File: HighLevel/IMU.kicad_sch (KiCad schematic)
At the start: 8 parts, among them U1 MPU-9150

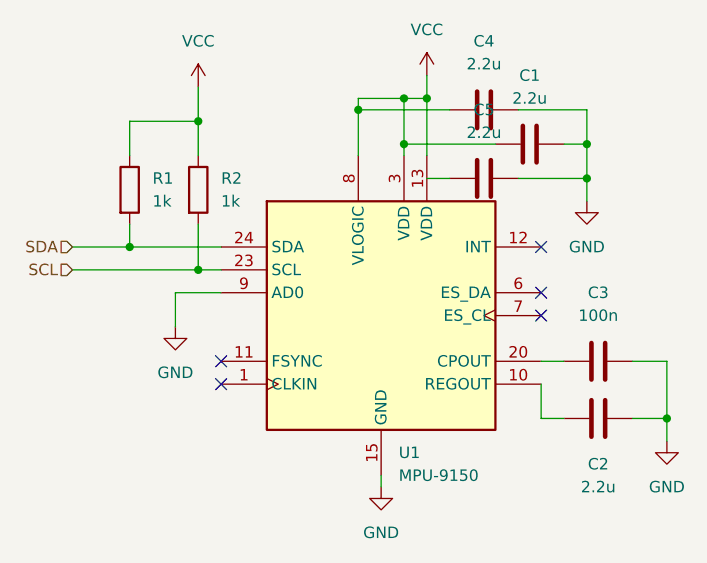
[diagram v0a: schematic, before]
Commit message: Arranged components on PCB
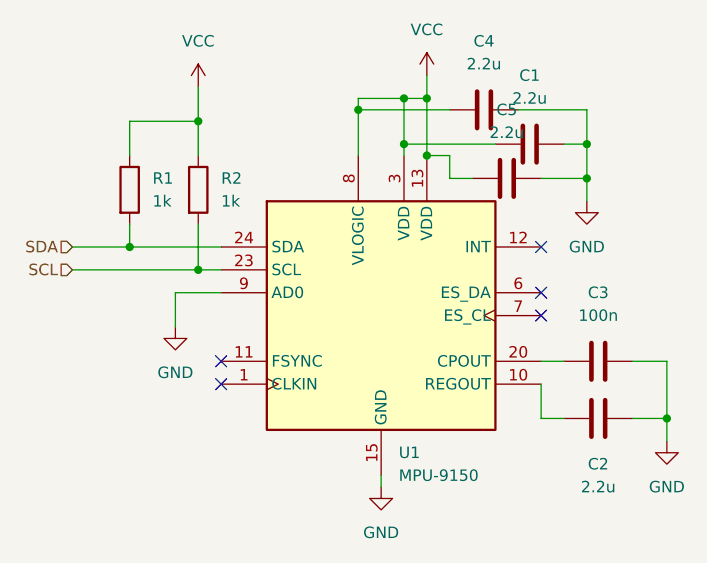
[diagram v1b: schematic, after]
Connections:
- net VCC: now also C5.1
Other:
- moved on the sheet: C5
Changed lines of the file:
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@@
   (junction (at 182.88 76.2) (diameter 0) (color 0 0 0 0)
+  )
+  (junction (at 165.1 73.66) (diameter 0) (color 0 0 0 0)
   )
   (junction (at 182.88 72.39) (diameter 0) (color 0 0 0 0)
@@
     (stroke (width 0) (type default))
   )
-  (wire (pts (xy 165.1 76.2) (xy 167.64 76.2))
+  (wire (pts (xy 167.64 76.2) (xy 170.18 76.2))
+    (stroke (width 0) (type default))
+  )
+  (wire (pts (xy 137.16 88.9) (xy 142.24 88.9))
+    (stroke (width 0) (type default))
+  )
+  (wire (pts (xy 139.7 81.28) (xy 139.7 86.36))
+    (stroke (width 0) (type default))
+  )
+  (wire (pts (xy 132.08 73.66) (xy 132.08 69.85))
+    (stroke (width 0) (type default))
+  )
+  (wire (pts (xy 162.56 67.31) (xy 165.1 67.31))
+    (stroke (width 0) (type default))
+  )
+  (wire (pts (xy 162.56 67.31) (xy 162.56 72.39))
+    (stroke (width 0) (type default))
+  )
+  (wire (pts (xy 182.88 76.2) (xy 182.88 78.74))
+    (stroke (width 0) (type default))
+  )
+  (wire (pts (xy 177.8 76.2) (xy 182.88 76.2))
+    (stroke (width 0) (type default))
+  )
+  (wire (pts (xy 177.8 102.87) (xy 180.34 102.87))
+    (stroke (width 0) (type default))
+  )
+  (wire (pts (xy 132.08 83.82) (xy 142.24 83.82))
+    (stroke (width 0) (type default))
+  )
+  (wire (pts (xy 132.08 69.85) (xy 139.7 69.85))
+    (stroke (width 0) (type default))
+  )
+  (wire (pts (xy 137.16 92.71) (xy 137.16 88.9))
+    (stroke (width 0) (type default))
+  )
+  (wire (pts (xy 132.08 81.28) (xy 132.08 83.82))
+    (stroke (width 0) (type default))
+  )
+  (wire (pts (xy 175.26 68.58) (xy 182.88 68.58))
+    (stroke (width 0) (type default))
+  )
+  (wire (pts (xy 157.48 67.31) (xy 157.48 68.58))
+    (stroke (width 0) (type default))
+  )
+  (wire (pts (xy 139.7 66.04) (xy 139.7 69.85))
+    (stroke (width 0) (type default))
+  )
+  (wire (pts (xy 177.8 99.06) (xy 177.8 102.87))
+    (stroke (width 0) (type default))
+  )
+  (wire (pts (xy 191.77 96.52) (xy 191.77 102.87))
+    (stroke (width 0) (type default))
+  )
+  (wire (pts (xy 182.88 68.58) (xy 182.88 72.39))
+    (stroke (width 0) (type default))
+  )
+  (wire (pts (xy 182.88 72.39) (xy 182.88 76.2))
+    (stroke (width 0) (type default))
+  )
+  (wire (pts (xy 187.96 102.87) (xy 191.77 102.87))
+    (stroke (width 0) (type default))
+  )
+  (wire (pts (xy 162.56 72.39) (xy 162.56 73.66))
+    (stroke (width 0) (type default))
+  )
+  (wire (pts (xy 165.1 64.77) (xy 165.1 67.31))
+    (stroke (width 0) (type default))
+  )
+  (wire (pts (xy 157.48 68.58) (xy 167.64 68.58))
+    (stroke (width 0) (type default))
+  )
+  (wire (pts (xy 191.77 102.87) (xy 191.77 105.41))
+    (stroke (width 0) (type default))
+  )
+  (wire (pts (xy 167.64 73.66) (xy 167.64 76.2))
+    (stroke (width 0) (type default))
+  )
+  (wire (pts (xy 157.48 67.31) (xy 162.56 67.31))
     (stroke (width 0) (type default))
   )
@@
     (stroke (width 0) (type default))
   )
-  (wire (pts (xy 137.16 88.9) (xy 142.24 88.9))
-    (stroke (width 0) (type default))
-  )
-  (wire (pts (xy 139.7 81.28) (xy 139.7 86.36))
-    (stroke (width 0) (type default))
-  )
-  (wire (pts (xy 132.08 73.66) (xy 132.08 69.85))
-    (stroke (width 0) (type default))
-  )
-  (wire (pts (xy 162.56 67.31) (xy 165.1 67.31))
-    (stroke (width 0) (type default))
-  )
-  (wire (pts (xy 162.56 67.31) (xy 162.56 72.39))
-    (stroke (width 0) (type default))
-  )
-  (wire (pts (xy 182.88 76.2) (xy 182.88 78.74))
-    (stroke (width 0) (type default))
-  )
-  (wire (pts (xy 175.26 76.2) (xy 182.88 76.2))
-    (stroke (width 0) (type default))
-  )
-  (wire (pts (xy 177.8 102.87) (xy 180.34 102.87))
-    (stroke (width 0) (type default))
-  )
-  (wire (pts (xy 132.08 83.82) (xy 142.24 83.82))
-    (stroke (width 0) (type default))
-  )
-  (wire (pts (xy 132.08 69.85) (xy 139.7 69.85))
-    (stroke (width 0) (type default))
-  )
-  (wire (pts (xy 137.16 92.71) (xy 137.16 88.9))
-    (stroke (width 0) (type default))
-  )
-  (wire (pts (xy 132.08 81.28) (xy 132.08 83.82))
-    (stroke (width 0) (type default))
-  )
-  (wire (pts (xy 175.26 68.58) (xy 182.88 68.58))
-    (stroke (width 0) (type default))
-  )
-  (wire (pts (xy 157.48 67.31) (xy 157.48 68.58))
-    (stroke (width 0) (type default))
-  )
-  (wire (pts (xy 139.7 66.04) (xy 139.7 69.85))
-    (stroke (width 0) (type default))
-  )
-  (wire (pts (xy 177.8 99.06) (xy 177.8 102.87))
-    (stroke (width 0) (type default))
-  )
-  (wire (pts (xy 191.77 96.52) (xy 191.77 102.87))
-    (stroke (width 0) (type default))
-  )
-  (wire (pts (xy 182.88 68.58) (xy 182.88 72.39))
-    (stroke (width 0) (type default))
-  )
-  (wire (pts (xy 182.88 72.39) (xy 182.88 76.2))
-    (stroke (width 0) (type default))
-  )
-  (wire (pts (xy 187.96 102.87) (xy 191.77 102.87))
-    (stroke (width 0) (type default))
-  )
-  (wire (pts (xy 162.56 72.39) (xy 162.56 73.66))
-    (stroke (width 0) (type default))
-  )
-  (wire (pts (xy 165.1 64.77) (xy 165.1 67.31))
-    (stroke (width 0) (type default))
-  )
-  (wire (pts (xy 157.48 68.58) (xy 167.64 68.58))
-    (stroke (width 0) (type default))
-  )
-  (wire (pts (xy 191.77 102.87) (xy 191.77 105.41))
-    (stroke (width 0) (type default))
-  )
-  (wire (pts (xy 157.48 67.31) (xy 162.56 67.31))
-    (stroke (width 0) (type default))
-  )
   (wire (pts (xy 125.73 86.36) (xy 139.7 86.36))
     (stroke (width 0) (type default))
@@
     (stroke (width 0) (type default))
   )
+  (wire (pts (xy 167.64 73.66) (xy 165.1 73.66))
+    (stroke (width 0) (type default))
+  )
+  (wire (pts (xy 162.56 72.39) (xy 172.72 72.39))
+    (stroke (width 0) (type default))
+  )
   (wire (pts (xy 125.73 83.82) (xy 132.08 83.82))
     (stroke (width 0) (type default))
@@
   )
   (wire (pts (xy 139.7 69.85) (xy 139.7 73.66))
-    (stroke (width 0) (type default))
-  )
-  (wire (pts (xy 162.56 72.39) (xy 172.72 72.39))
     (stroke (width 0) (type default))
   )
@@
     )
   )
-  (symbol (lib_id "Device:C") (at 171.45 76.2 90) (unit 1)
-    (in_bom yes) (on_board yes) (dnp no) (fields_autoplaced)
-    (property "Reference" "C5" (at 171.45 68.58 90)
-      (effects (font (size 1.27 1.27)))
-    )
-    (property "Value" "2.2u" (at 171.45 71.12 90)
-      (effects (font (size 1.27 1.27)))
-    )
-    (property "Footprint" "Capacitor_SMD:C_0805_2012Metric" (at 175.26 75.2348 0)
-      (effects (font (size 1.27 1.27)) hide)
-    )
-    (property "Datasheet" "~" (at 171.45 76.2 0)
-      (effects (font (size 1.27 1.27)) hide)
-    )
+  (symbol (lib_id "Device:C") (at 173.99 76.2 90) (unit 1)
+    (in_bom yes) (on_board yes) (dnp no) (fields_autoplaced)
+    (property "Reference" "C5" (at 173.99 68.58 90)
+      (effects (font (size 1.27 1.27)))
+    )
+    (property "Value" "2.2u" (at 173.99 71.12 90)
+      (effects (font (size 1.27 1.27)))
+    )
+    (property "Footprint" "Capacitor_SMD:C_0805_2012Metric" (at 177.8 75.2348 0)
+      (effects (font (size 1.27 1.27)) hide)
+    )
+    (property "Datasheet" "~" (at 173.99 76.2 0)
+      (effects (font (size 1.27 1.27)) hide)
+    )
